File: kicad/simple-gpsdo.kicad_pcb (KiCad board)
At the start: 2 copper layers, 119.5 x 74.5 mm, 90 parts, among them J1 PPS_OUT, J2 PWR, J3 ISP, J6 USB_B_Micro, J7 NEO-6M, J8 10MHz_OUT, Q1 DMP3099L, SW1 RST, U1 BD50FC0FP-E2, U2 ATmega32U4-AU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

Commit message: Changed input fuse from 3A to 2A
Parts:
- F1: value 3A -> 2A
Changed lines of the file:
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@@
       (effects (font (size 1 1) (thickness 0.15)))
     )
-    (fp_text value 3A (at 0 1.82) (layer F.Fab)
+    (fp_text value 2A (at 0 1.82) (layer F.Fab)
       (effects (font (size 1 1) (thickness 0.15)))
     )

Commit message: finalized rev D schematic
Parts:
- removed G***: LOGO, w3axl-logos:logo-4.2x4.2
- added R19: 10k, Resistor_SMD:R_0805_2012Metric_Pad1.15x1.40mm_HandSolder, F.Cu at (141.5, 143.8)
- added R21: 10k, Resistor_SMD:R_0805_2012Metric_Pad1.15x1.40mm_HandSolder, F.Cu at (137.5, 136.0)
- added R22: 65k, Resistor_SMD:R_0805_2012Metric_Pad1.15x1.40mm_HandSolder, F.Cu at (141.5, 139.2)
- Q1: value DMP3099L -> PJA3407
- U1: value BD50FC0FP-E2 -> XRP6272ITC5TR-F; footprint Package_TO_SOT_SMD:TO-252-2 -> Package_TO_SOT_SMD:TO-252-5_TabPin3
- moved C30 3.55 mm to (144.5, 138.6), turned to 90 degrees
- moved U1 1.35 mm to (133.8, 141.2)
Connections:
- U1 pad 1: +6V -> Net-(R19-Pad2)
- U1 pad 2: GND -> +6V
- U1 pad 3: +5V -> GND
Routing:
- net +6V: track 27.7 -> 16.7 mm
- net +5V: track 287.7 -> 294.5 mm
- net Net-(R21-Pad1): track 0.00 -> 6.10 mm
- net Net-(R19-Pad2): track 0.00 -> 3.98 mm
- net GND: vias 348 -> 386
- added copper zone on F.Cu, net +5V
- added copper zone on F.Cu, net +6V

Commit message: finalized schematic and PCB
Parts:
- moved TP1 24.2 mm to (190.2, 107.3)
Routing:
- net GPS_PPS: track 158.7 -> 165.5 mm

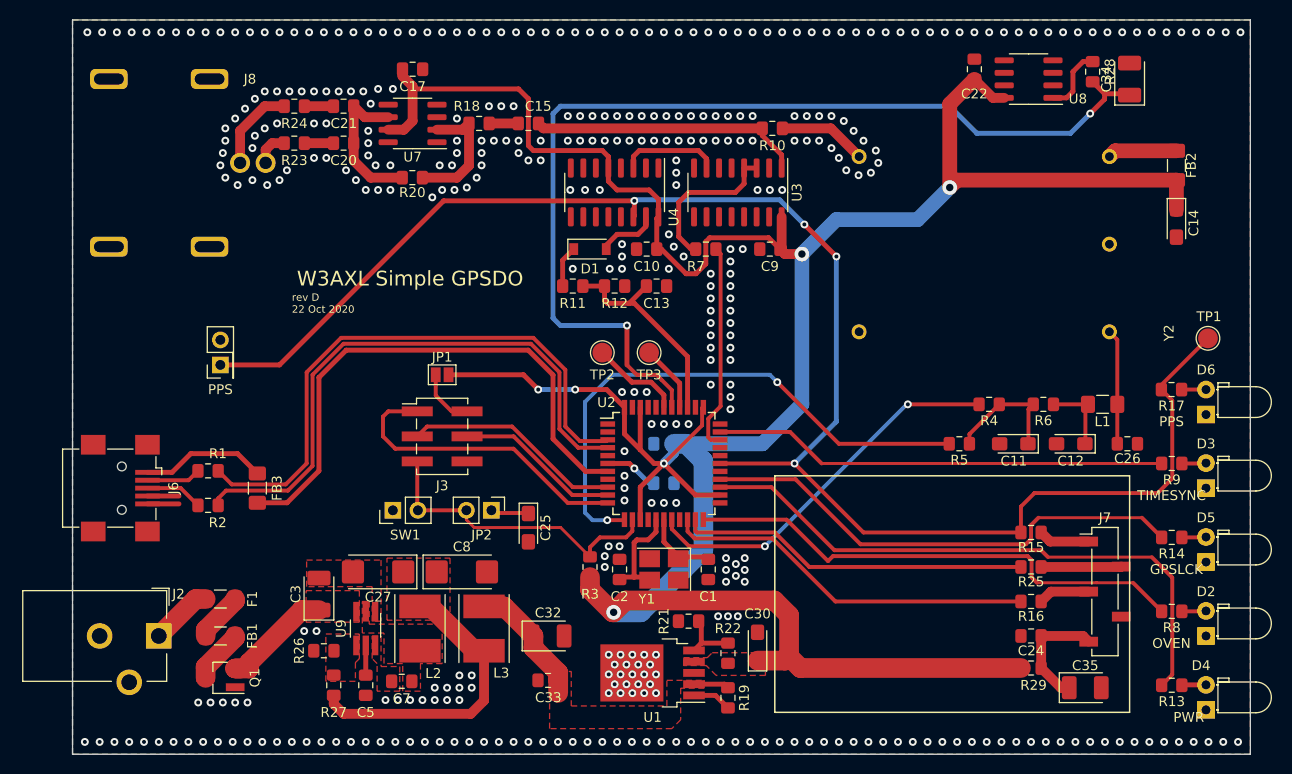
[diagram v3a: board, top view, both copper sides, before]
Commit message: revision E updates
added external 1.2 VREF
connected UVCC to VCC
switched pins for 5MHz, PPS, and LEDs to work properly
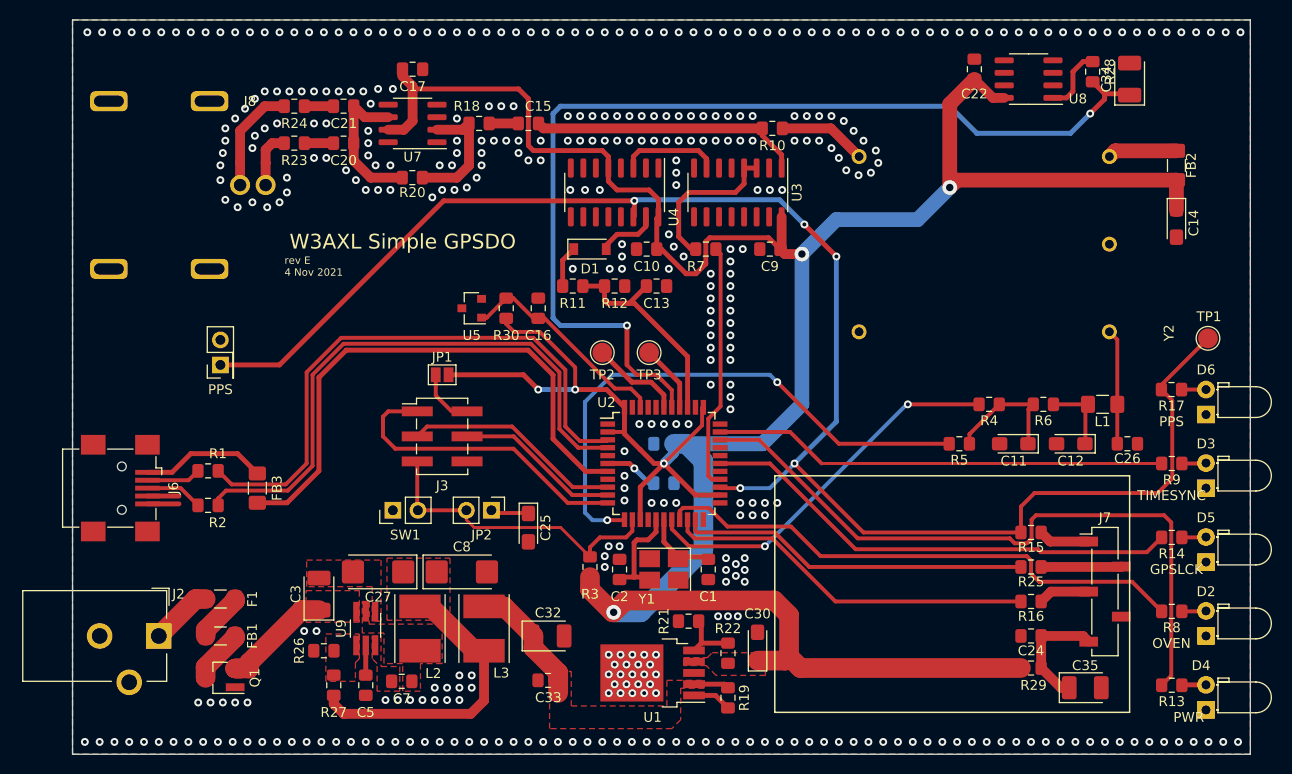
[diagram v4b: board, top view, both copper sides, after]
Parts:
- added C16: 0.1uF, Capacitor_SMD:C_0805_2012Metric_Pad1.15x1.40mm_HandSolder, F.Cu at (122.2, 104.2)
- added R30: 10k, Resistor_SMD:R_0805_2012Metric_Pad1.15x1.40mm_HandSolder, F.Cu at (119.0, 104.2)
- added U5: LM4041QDIM3-1.2, Package_TO_SOT_SMD:SOT-23, F.Cu at (115.5, 104.2)
- moved J8 2.25 mm to (92.0, 91.8)
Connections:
- net ADC1 renamed Net-(TP3-Pad1)
- net ADC3 renamed Net-(TP2-Pad1)
- U2 pad 19: Net-(U2-Pad19) -> OVEN_TEMP
- U2 pad 2: Net-(U2-Pad2) -> +5V
- U2 pad 22: OVEN_TEMP -> Net-(U2-Pad22)
- U2 pad 25: POWER_OK -> GPS_PPS
- U2 pad 26: GPS_LOCK -> 5MHz
- U2 pad 28: GPS_PPS -> GPS_LOCK
- U2 pad 31: 5MHz -> POWER_OK
- U2 pad 42: +5V -> Net-(C16-Pad2)
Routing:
- net Net-(C16-Pad2): track 0.00 -> 22.1 mm
- net +5V: track 294.5 -> 303.7 mm
- net POWER_OK: track 61.0 -> 69.7 mm
- net 5MHz: track 21.1 -> 25.1 mm
- net OVEN_TEMP: track 51.8 -> 55.0 mm
- net Net-(J8-Pad2): track 8.76 -> 11.0 mm
- net Net-(J8-Pad1): track 3.50 -> 5.75 mm
- net GPS_LOCK: track 50.3 -> 49.1 mm
- net GPS_PPS: track 165.5 -> 166.5 mm, vias 4 -> 5
- net GND: vias 386 -> 393
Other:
- board text added: "rev E 4 Nov 2021"
- board text removed: "rev D 22 Oct 2020"

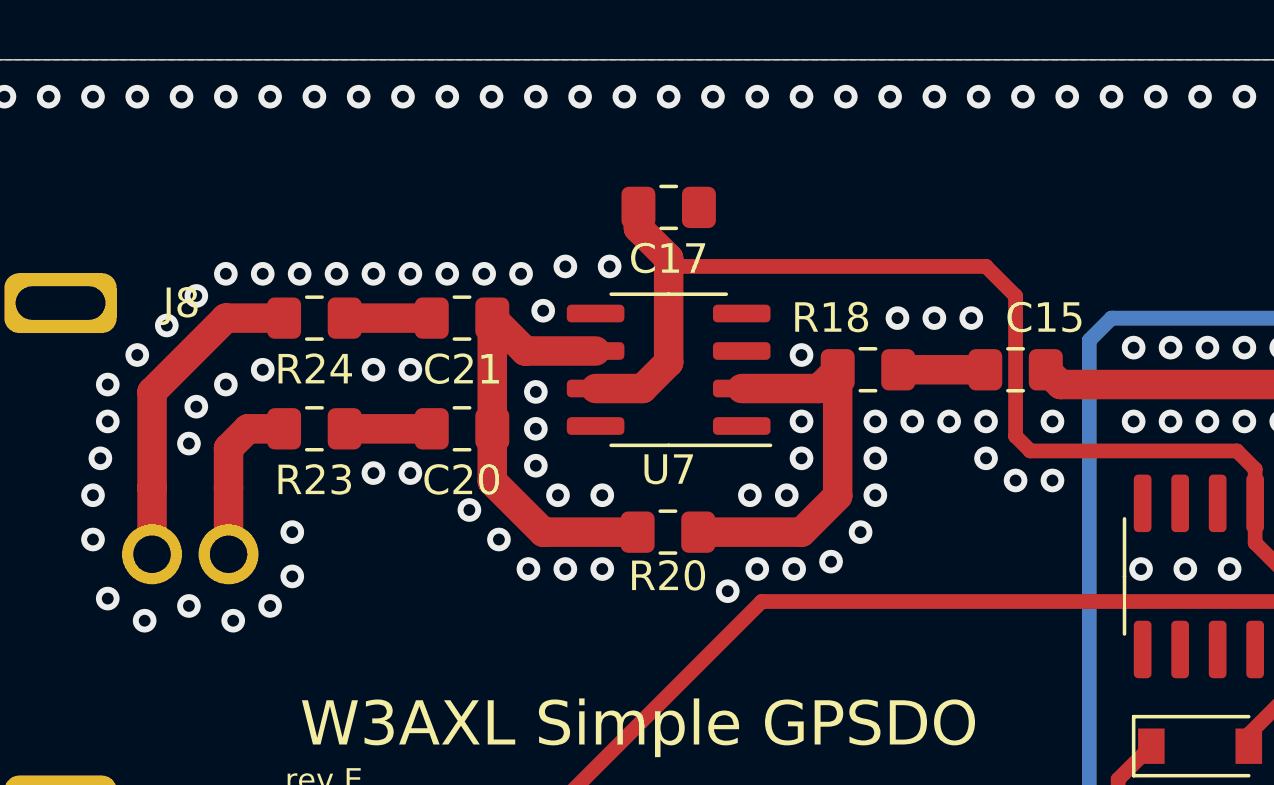
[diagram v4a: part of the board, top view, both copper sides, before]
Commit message: final schematic updates for new buffer amplifier
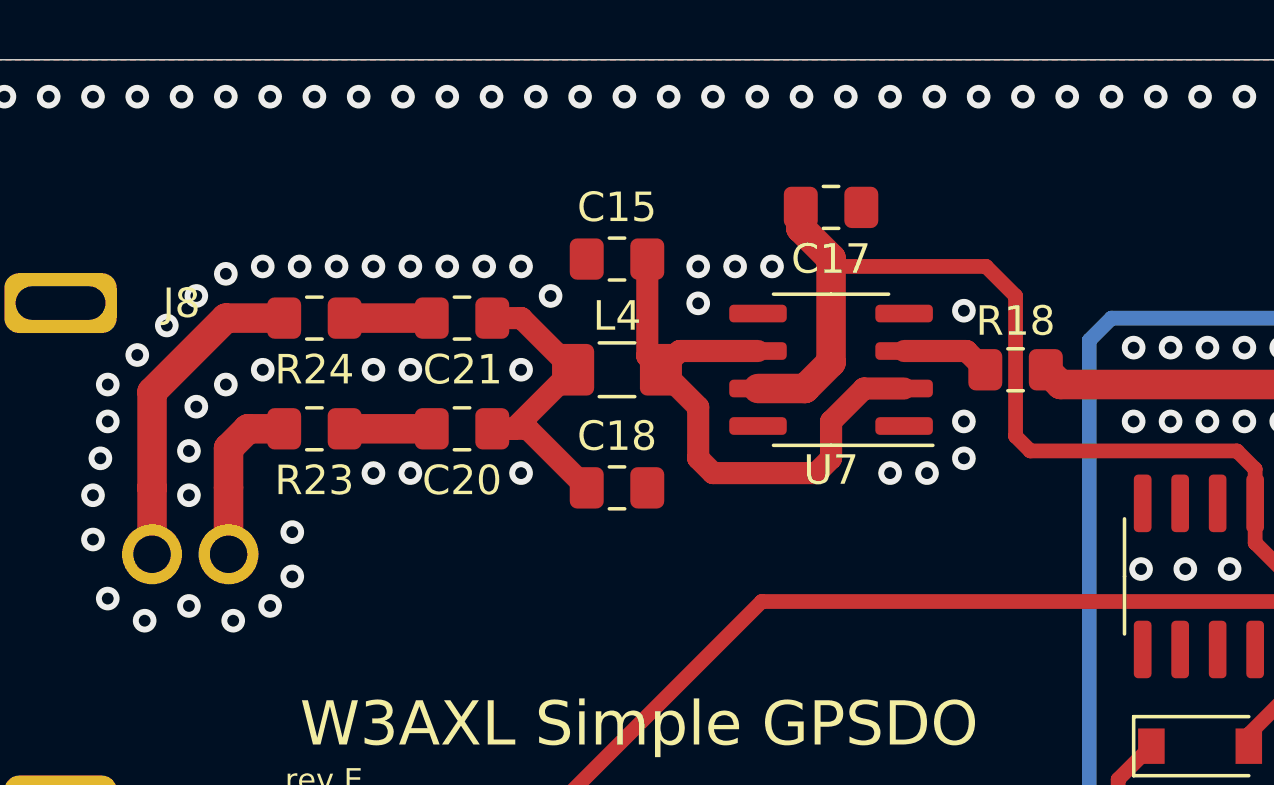
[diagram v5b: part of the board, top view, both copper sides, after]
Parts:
- removed R20: 10k, Resistor_SMD:R_0805_2012Metric_Pad1.15x1.40mm_HandSolder
- added C18: 430pF, Capacitor_SMD:C_0805_2012Metric_Pad1.15x1.40mm_HandSolder, F.Cu at (107.8, 89.5)
- added L4: 470nH, Inductor_SMD:L_1206_3216Metric_Pad1.42x1.75mm_HandSolder, F.Cu at (107.8, 85.5)
- C15: value 0.1uF -> 750pF
- R18: value 10k -> 50R
- U7: value LM7171 -> TLV3541IDR
- moved C15 14.0 mm to (107.8, 81.8)
- moved C17 5.50 mm to (115.0, 80.0)
- moved U7 5.50 mm to (115.0, 85.5)
- moved R18 5.00 mm to (121.2, 85.5)
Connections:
- C15 pad 1: Net-(C15-Pad1) -> GND
- C15 pad 2: 10MHz -> Net-(C15-Pad2)
- C20 pad 2: Net-(C20-Pad2) -> Net-(C18-Pad2)
- C21 pad 2: Net-(C20-Pad2) -> Net-(C18-Pad2)
- R18 pad 2: Net-(C15-Pad1) -> 10MHz
- U7 pad 2: Net-(R18-Pad1) -> Net-(C15-Pad2)
- U7 pad 3: GND -> Net-(R18-Pad1)
- U7 pad 6: Net-(C20-Pad2) -> Net-(C15-Pad2)
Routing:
- net Net-(C15-Pad2): track 0.00 -> 20.1 mm
- net Net-(C20-Pad2): track 15.1 -> 0.00 mm
- net Net-(C18-Pad2): track 0.00 -> 11.1 mm
- net Net-(R18-Pad1): track 13.0 -> 3.01 mm
- net +5V: track 303.7 -> 298.2 mm
- net Net-(C15-Pad1): track 2.95 -> 0.00 mm
- net GND: vias 393 -> 370

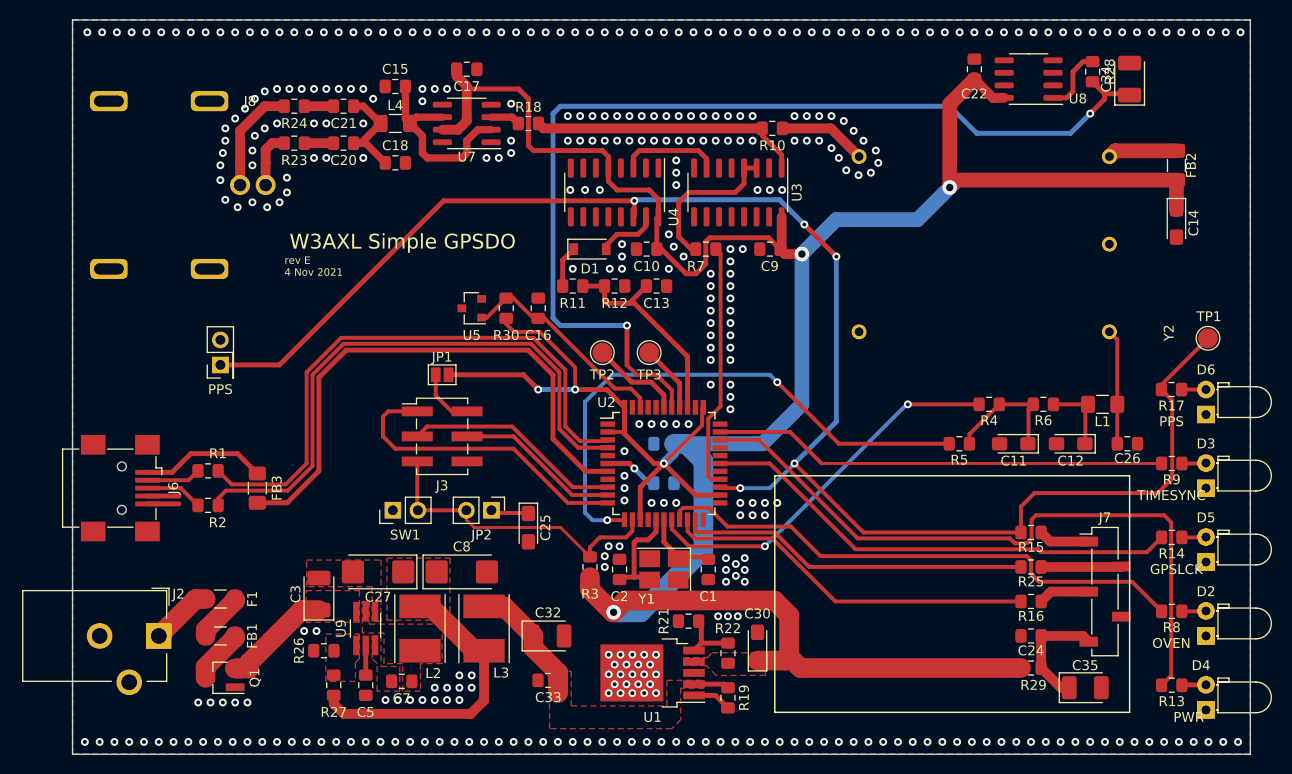
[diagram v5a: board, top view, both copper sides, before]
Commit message: more schematic and pcb updates
finished 10MHz output and fixed LED orientation
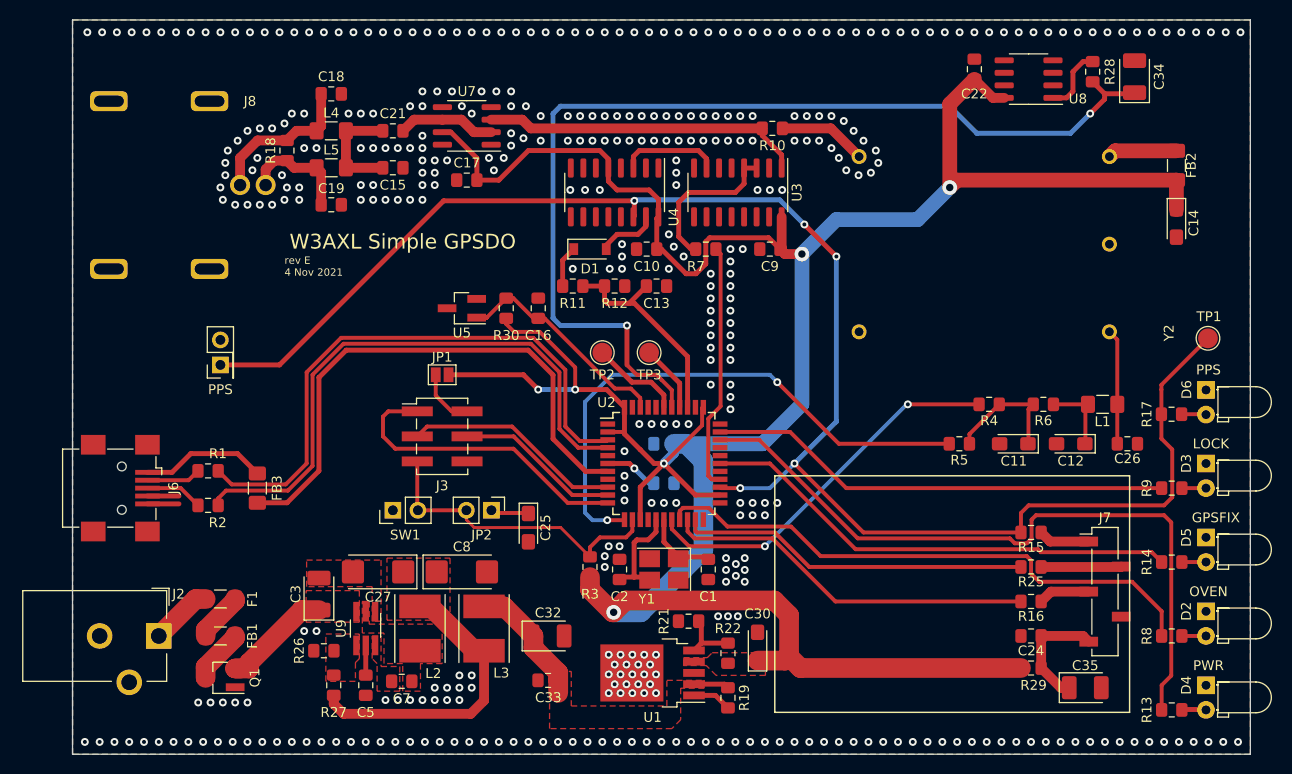
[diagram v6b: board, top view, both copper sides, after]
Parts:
- removed C20: 0.1uF, Capacitor_SMD:C_0805_2012Metric_Pad1.15x1.40mm_HandSolder
- removed R23, R24: 50R, Resistor_SMD:R_0805_2012Metric_Pad1.15x1.40mm_HandSolder
- added C19: 330pF, Capacitor_SMD:C_0805_2012Metric_Pad1.15x1.40mm_HandSolder, F.Cu at (101.2, 93.8)
- added L5: 1uH, Inductor_SMD:L_1206_3216Metric_Pad1.42x1.75mm_HandSolder, F.Cu at (101.2, 90.0)
- C15: value 750pF -> 330pF
- C18: value 430pF -> 330pF
- D2, D3, D4, D5, D6: footprint LED_THT:LED_D3.0mm_Horizontal_O1.27mm_Z2.0mm_Clear -> LED_THT_CUSTOM:LED_D3.0mm_Horizontal_O1.27mm_Z2.0mm
- L4: value 470nH -> 1uH
- R18: value 50R -> 100
- U5: footprint Package_TO_SOT_SMD:SOT-23 -> Package_TO_SOT_SMD:SOT-23_Handsoldering
- moved R18 24.7 mm to (96.8, 88.2), turned to 90 degrees
- moved C17 11.2 mm to (115.0, 91.2), turned to 0 degrees
- moved C18 9.55 mm to (101.2, 82.5)
- moved C15 8.25 mm to (107.5, 90.0), turned to 180 degrees
- moved L4 6.54 mm to (101.2, 86.2)
- moved C21 5.59 mm to (107.5, 86.2)
- moved R13 2.50 mm to (186.5, 145.0)
- moved R14 2.50 mm to (186.5, 130.0)
- moved R17 2.50 mm to (186.5, 115.0)
- moved R8 2.50 mm to (186.5, 137.5)
- moved R9 2.50 mm to (186.5, 122.5)
- moved U5 1.00 mm to (114.5, 104.2)
- moved C34 0.56 mm to (182.8, 80.8)
- moved U7 0.25 mm to (115.0, 85.8)
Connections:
- C21 pad 1: Net-(C21-Pad1) -> Net-(C15-Pad2)
- C21 pad 2: Net-(C18-Pad2) -> Net-(C21-Pad2)
- J8 pad 1: Net-(J8-Pad1) -> Net-(C19-Pad1)
- J8 pad 2: Net-(J8-Pad2) -> Net-(C18-Pad2)
- R18 pad 1: Net-(R18-Pad1) -> Net-(C19-Pad1)
- R18 pad 2: 10MHz -> Net-(C18-Pad2)
- U7 pad 2: Net-(C15-Pad2) -> Net-(C21-Pad2)
- U7 pad 3: Net-(R18-Pad1) -> 10MHz
- U7 pad 6: Net-(C15-Pad2) -> Net-(C21-Pad2)
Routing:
- net Net-(C19-Pad1): track 0.00 -> 11.4 mm
- net Net-(J8-Pad2): track 11.0 -> 0.00 mm
- net Net-(C21-Pad2): track 0.00 -> 9.95 mm
- net Net-(C15-Pad2): track 20.1 -> 11.2 mm
- net +5V: track 298.2 -> 291.1 mm
- net Net-(J8-Pad1): track 5.75 -> 0.00 mm
- net 10MHz: track 27.7 -> 32.7 mm
- net Net-(C18-Pad2): track 11.1 -> 15.6 mm
- net Net-(R18-Pad1): track 3.01 -> 0.00 mm
- net Net-(C21-Pad1): track 2.95 -> 0.00 mm
- net Net-(C20-Pad1): track 2.95 -> 0.00 mm
- net POWER_OK: track 69.7 -> 72.2 mm
- net OVEN_TEMP: track 55.0 -> 57.5 mm
- net TIME_LOCK: track 46.1 -> 47.2 mm
- net Net-(C16-Pad2): track 22.1 -> 23.1 mm
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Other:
- board text added: "GPSFIX"
- board text added: "LOCK"
- board text removed: "GPSLCK"
- board text removed: "TIMESYNC"

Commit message: schematic for rev E finalized
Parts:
- R30: value 10k -> 3k9
- U5: value LM4041QDIM3-1.2 -> LM4041DFTA
